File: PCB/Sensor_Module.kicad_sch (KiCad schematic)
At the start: 16 parts, among them J3 Conn_01x01_Pin, J4 Conn_01x02_Pin, U4 VL6180

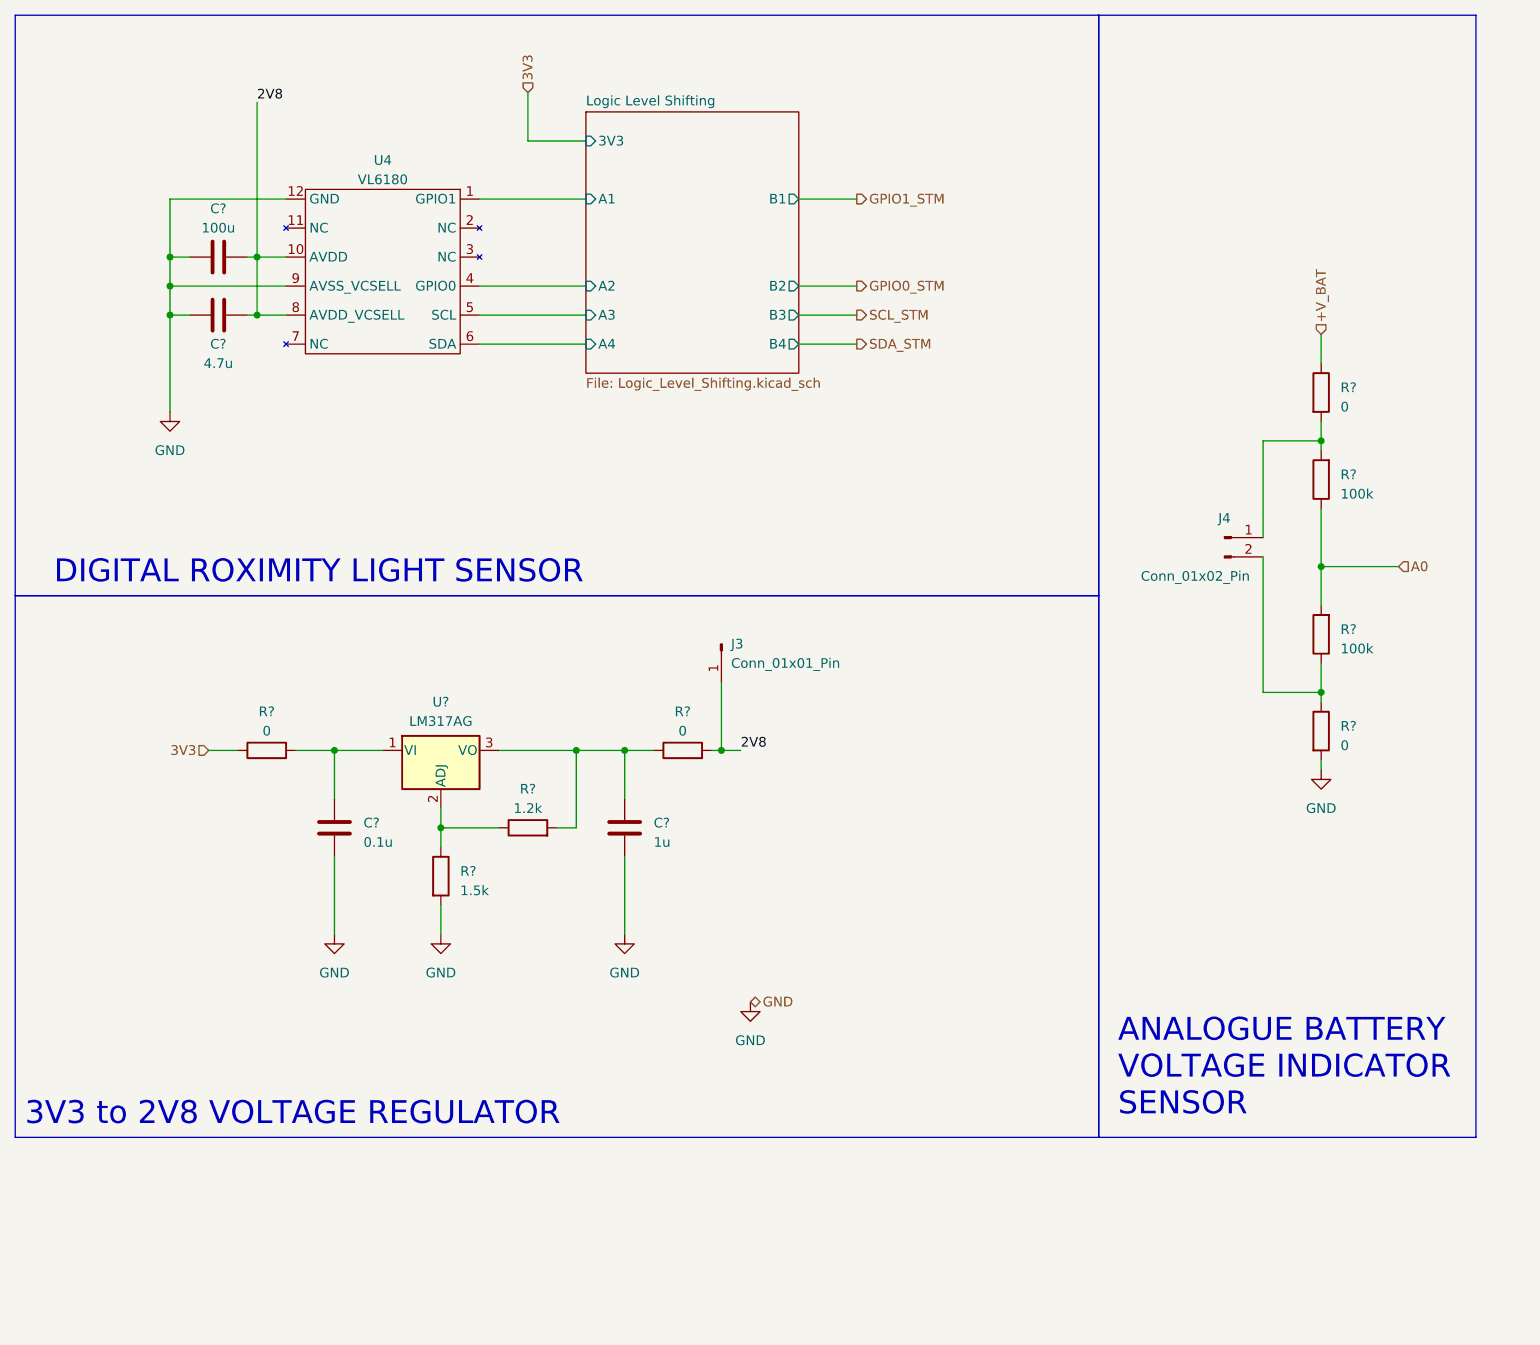
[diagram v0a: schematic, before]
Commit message: literally all the footprints
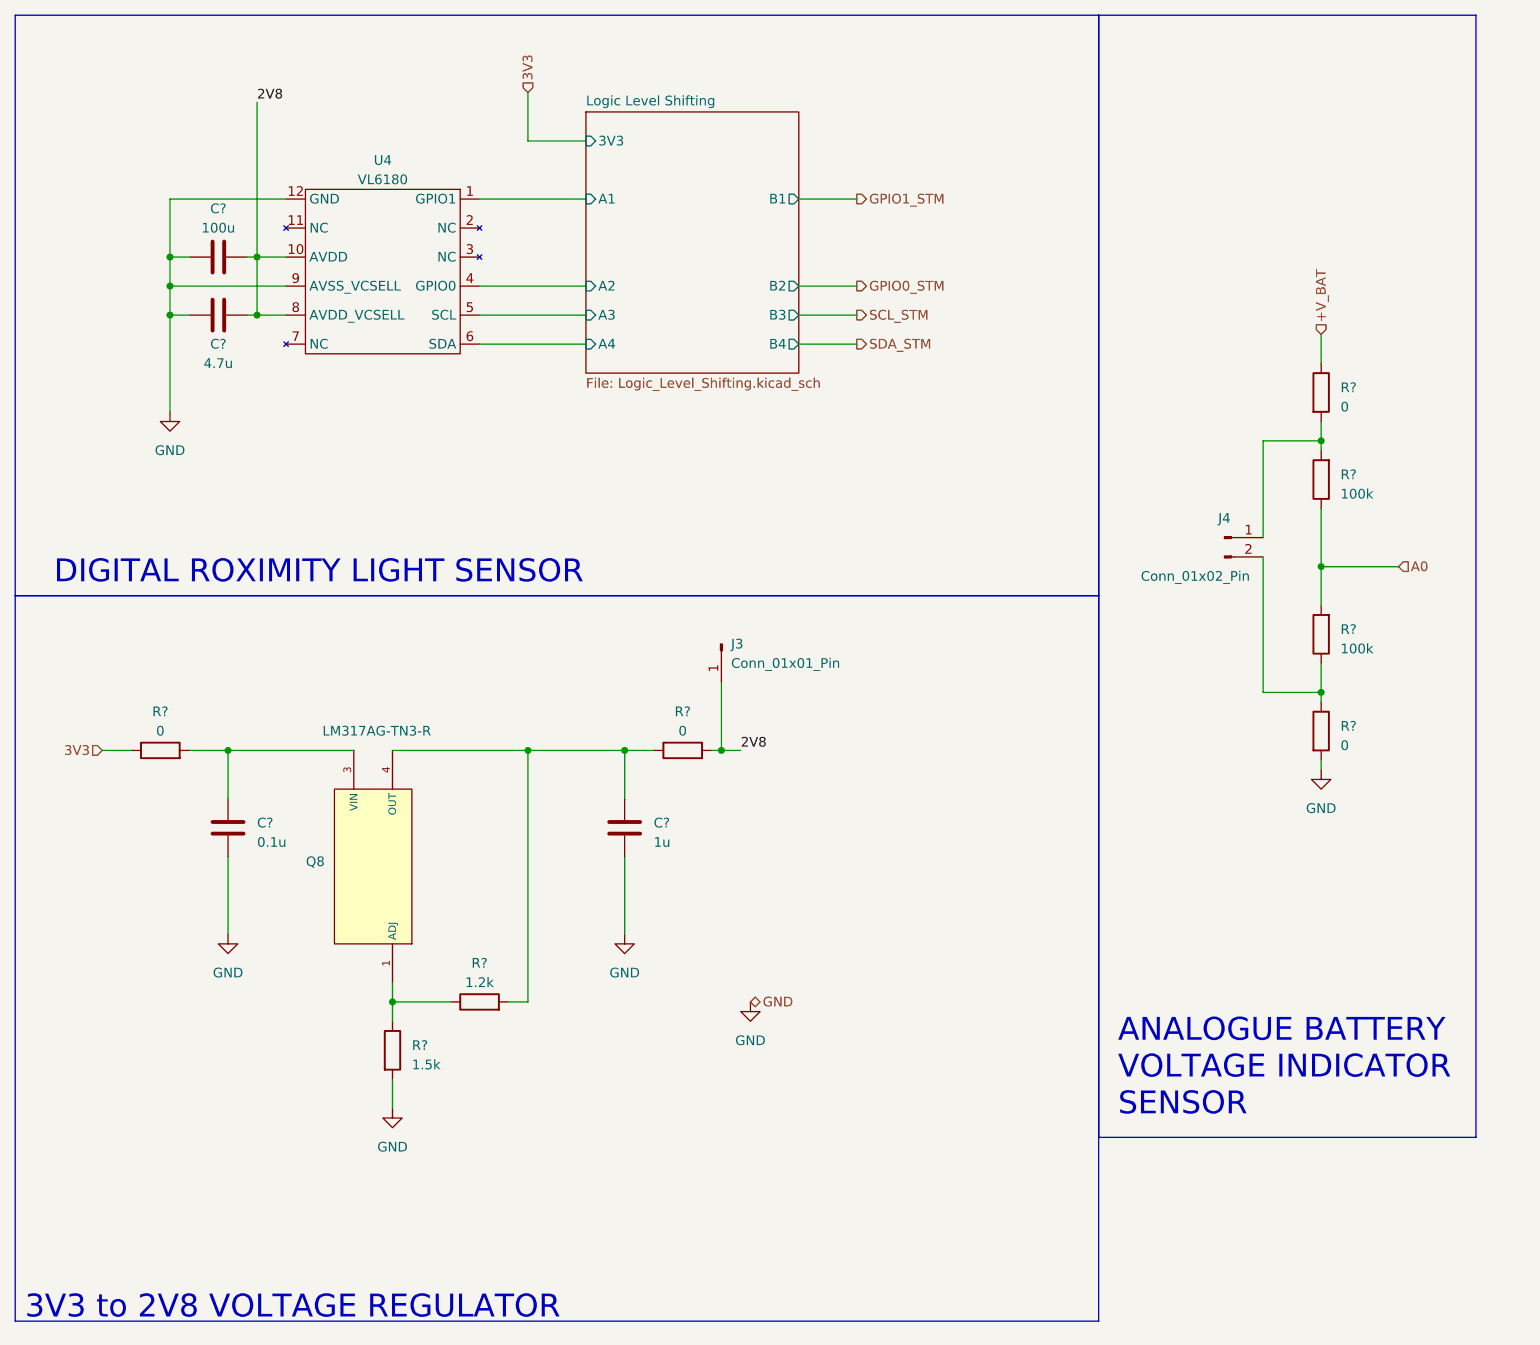
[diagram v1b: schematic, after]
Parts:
- removed U?: LM317AG, Package_TO_SOT_THT:TO-39-3, symbol Regulator_Linear:LM317MD
- added Q8: LM317AG-TN3-R, JLC_Misc:TO-252-2_L6.5-W6.1-P4.58-LS10.0-TL, symbol My_Schematic_lib:LM317AG-TN3-R
- C?: footprint (none) -> JLC:C1206
- C?: footprint (none) -> JLC:C0603
- C?: footprint (none) -> JLC:C0805
- C?: footprint (none) -> JLC:C0402_NEW
- J3: footprint (none) -> Connector_PinSocket_2.54mm:PinSocket_1x01_P2.54mm_Vertical
- J4: footprint (none) -> Connector_PinSocket_2.54mm:PinSocket_1x02_P2.54mm_Vertical
- R? (x8): footprint (none) -> Resistor_SMD:R_0805_2012Metric
- U4: footprint (none) -> JLC_Prox:LGA-12_L4.8-W2.8-P0.75-BL
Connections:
- net at C?.2, R?.2: now also Q8.3 (VIN)
- net at R?.1, R?.1: now also Q8.1 (ADJ)
- net at C?.2, R?.1, R?.2: now also Q8.4 (OUT)
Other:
- moved on the sheet: C?, R?

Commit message: Pins not Sockets
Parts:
- J3: footprint Connector_PinSocket_2.54mm:PinSocket_1x01_P2.54mm_Vertical -> Connector_PinHeader_2.54mm:PinHeader_1x01_P2.54mm_Vertical
- J4: footprint Connector_PinSocket_2.54mm:PinSocket_1x02_P2.54mm_Vertical -> Connector_PinHeader_2.54mm:PinHeader_1x02_P2.54mm_Vertical
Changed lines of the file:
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@@
       (effects (font (size 1.27 1.27)))
     )
-    (property "Footprint" "Connector_PinSocket_2.54mm:PinSocket_1x02_P2.54mm_Vertical" (at 171.45 81.28 0)
+    (property "Footprint" "Connector_PinHeader_2.54mm:PinHeader_1x02_P2.54mm_Vertical" (at 171.45 81.28 0)
       (effects (font (size 1.27 1.27)) hide)
     )
@@
       (effects (font (size 1.27 1.27)) (justify left))
     )
-    (property "Footprint" "Connector_PinSocket_2.54mm:PinSocket_1x01_P2.54mm_Vertical" (at 105.41 95.25 0)
-      (effects (font (size 1.27 1.27)) hide)
-    )
+    (property "Footprint" "Connector_PinHeader_2.54mm:PinHeader_1x01_P2.54mm_Vertical" (at 105.41 95.25 0)
+      (effects (font (size 1.27 1.27)) hide)
+    )
